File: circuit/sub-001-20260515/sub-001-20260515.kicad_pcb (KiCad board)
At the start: 2 copper layers, 114.3 x 107 mm, 148 parts, among them J1 Conn_NeoPixel, J2 Conn_SW_TGL, J3 Conn_Power, J4 Conn_Main, Q1 BSS138, Q2 BSS138, Q3 BSS138, Q4 BSS138, Q5 BSS138, Q6 BSS138, Q7 BSS138, Q8 BSS138, U11 LM1117GS-3.3, U12 NE555DR, U13 NE555DR, U14 LM1117GS-3.3, U15 LM1117GS-3.3, U18 NE555DR, U19 NE555DR, U2 LM1117GS-3.3, U20 TSSP58038, U21 TSSP58038, U22 NE555DR, U23 NE555DR, U24 TSSP58038, U25 TSSP58038, U26 HC-SR04, U27 HC-SR04, U28 HC-SR04, U29 HC-SR04, U4 NE555DR, U5 NE555DR, U7 LM1117GS-3.3, U9 LM1117MP-3.3

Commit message: Update サブ基板のPCBを進めた
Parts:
- moved U14 96.0 mm to (48.0, 0.00), turned to -90 degrees
- moved U7 96.0 mm to (-48.0, 0.00)
- moved U27 74.3 mm to (-37.0, 3.81), turned to 180 degrees
- moved U29 74.3 mm to (36.9, -3.81), turned to 0 degrees
- moved U3 64.4 mm to (-32.2, -1.17), turned to 180 degrees
- moved U8 64.4 mm to (32.2, -2.83), turned to 0 degrees

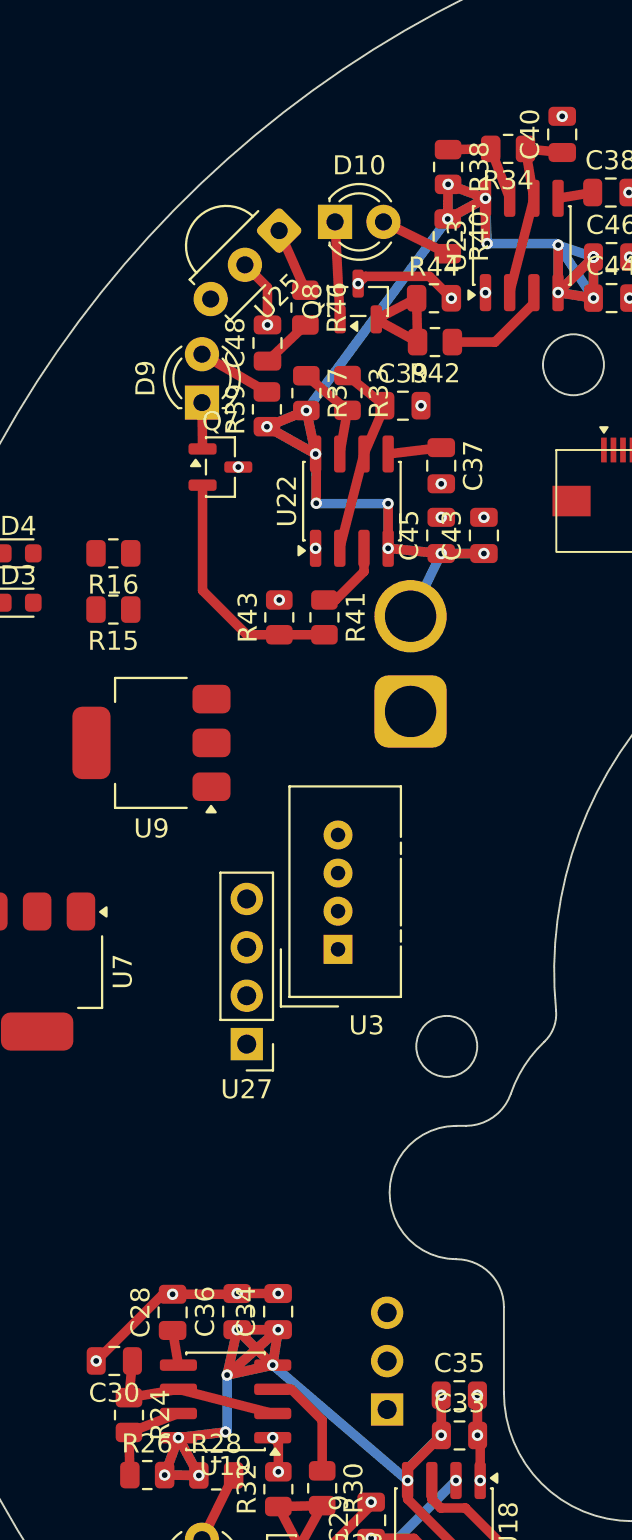
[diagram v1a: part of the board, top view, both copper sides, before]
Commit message: Update サブ基板のPCBを進めた
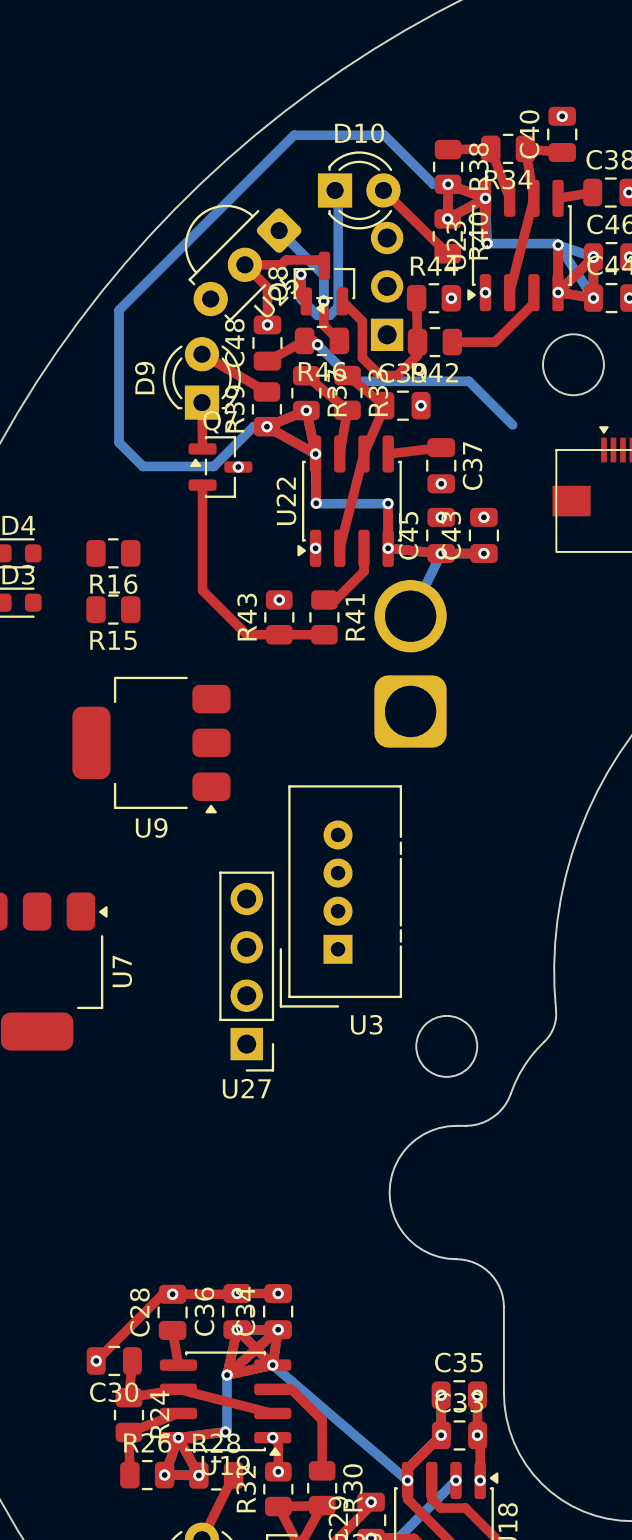
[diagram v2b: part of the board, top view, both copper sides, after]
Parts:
- moved J2 56.4 mm to (-29.6, -33.4)
- moved Q8 2.00 mm to (-32.9, -36.1)
- moved R46 1.95 mm to (-33.0, -33.1), turned to 180 degrees
- moved D10 1.65 mm to (-32.4, -41.0)
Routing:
- net +5V: track 370.8 -> 396.5 mm
- net IR_sig4: track 2.75 -> 15.0 mm, vias 0 -> 1
- net Net-(D10-K): track 5.12 -> 11.5 mm, vias 0 -> 1
- net Net-(U25-OUT): track 3.42 -> 7.10 mm, vias 0 -> 1
- net Net-(Q8-G): track 7.16 -> 10.1 mm
- net GND: track 79.1 -> 77.9 mm, vias 59 -> 58
- net Net-(D10-A): track 3.76 -> 4.73 mm

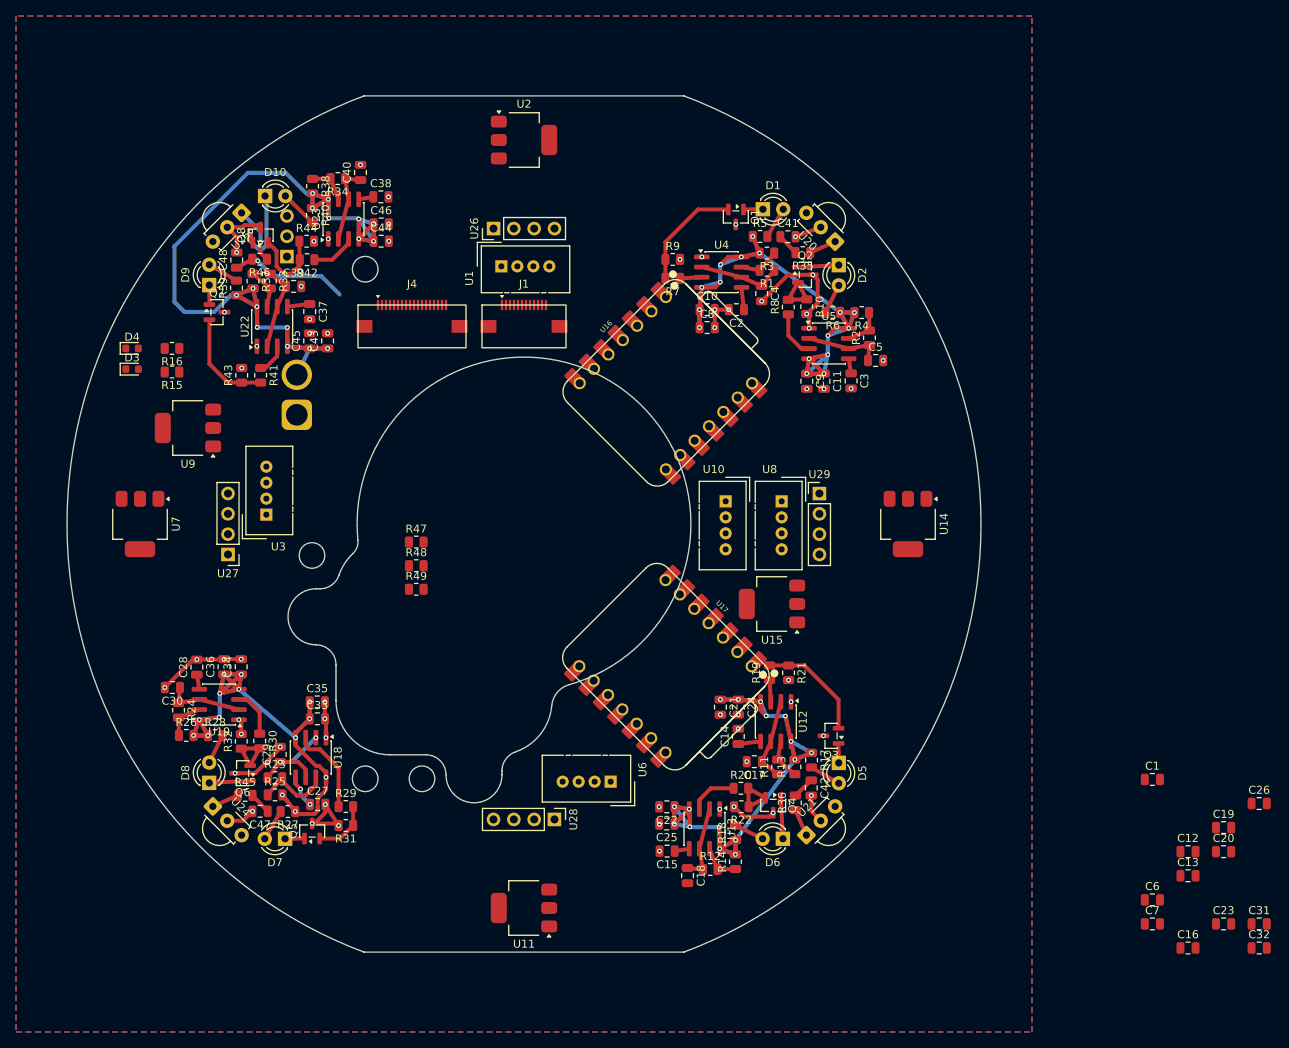
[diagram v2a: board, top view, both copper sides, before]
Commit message: Update サブ基板のFPCコネクタ周りを更新
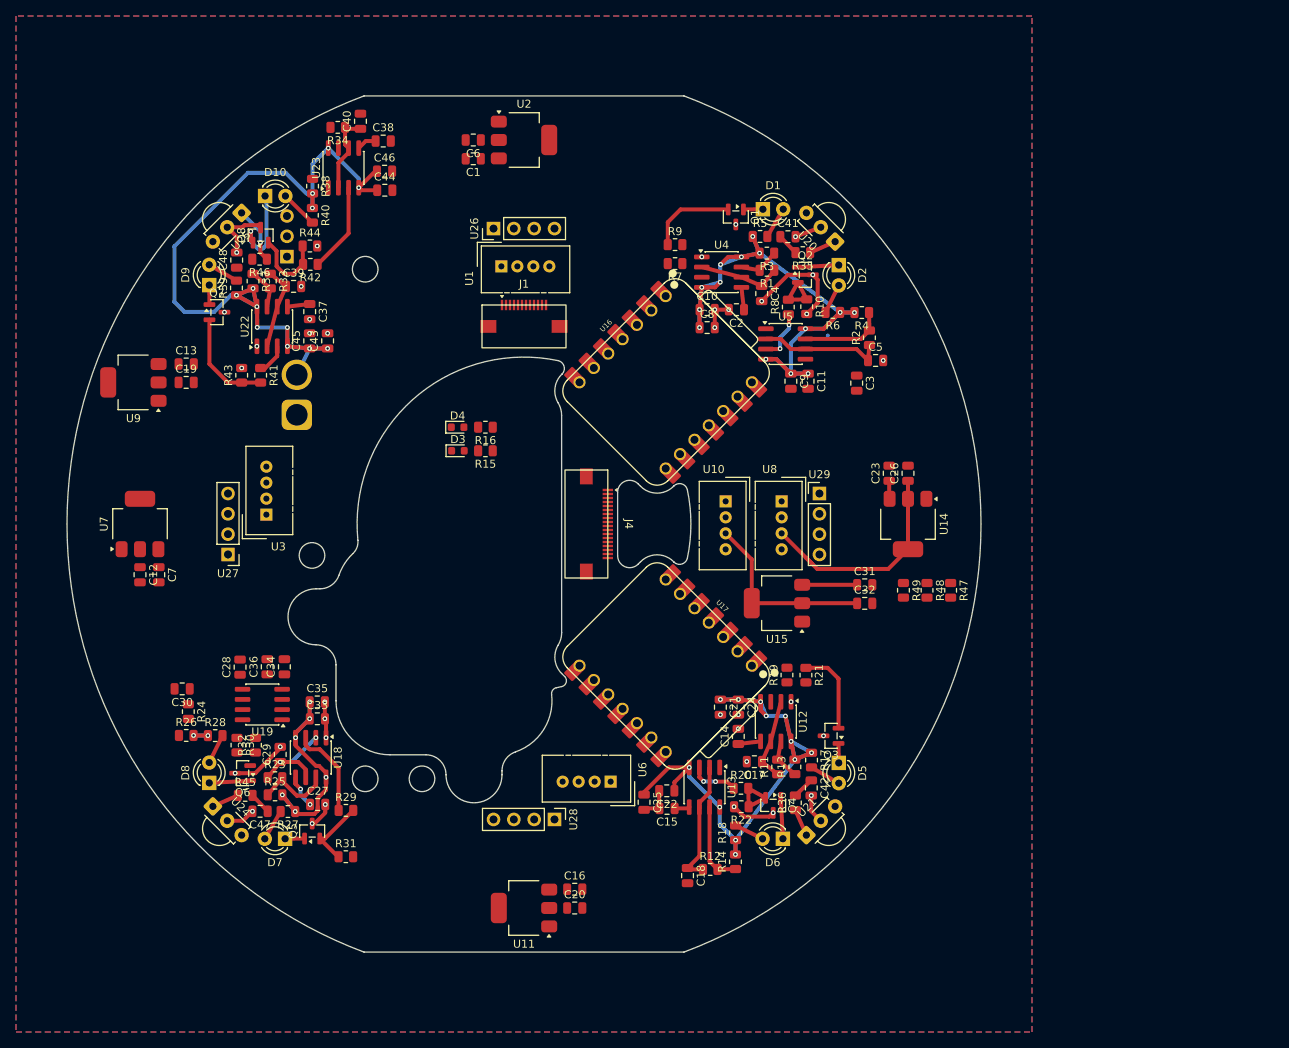
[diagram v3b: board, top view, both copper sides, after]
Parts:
- moved C19 141.1 mm to (-42.2, -17.7)
- moved C13 140.6 mm to (-42.2, -20.0)
- moved C12 135.5 mm to (-48.0, 6.34), turned to -90 degrees
- moved C7 131.6 mm to (-45.6, 6.34), turned to -90 degrees
- moved C6 127.4 mm to (-6.34, -48.0), turned to 180 degrees
- moved C1 115.0 mm to (-6.34, -45.6), turned to 180 degrees
- moved C20 81.4 mm to (6.34, 48.0)
- moved C16 77.0 mm to (6.34, 45.6)
- moved C23 70.1 mm to (45.6, -6.34), turned to 90 degrees
- moved R47 67.1 mm to (53.3, 8.29), turned to -90 degrees
- moved C32 65.5 mm to (42.6, 9.92)
- moved C31 65.0 mm to (42.6, 7.60)
- moved R48 63.9 mm to (50.4, 8.29), turned to -90 degrees
- moved R49 60.9 mm to (47.4, 8.29), turned to -90 degrees
- moved C26 60.3 mm to (48.0, -6.34), turned to 90 degrees
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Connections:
- C13 pad 2: Net-(C13-Pad2) -> GND
- C19 pad 2: Net-(C13-Pad2) -> GND
- J1 pad 1: +5V -> SIG_{NeoPixel}
- J1 pad 10: SW_{TCT3} -> +3.3V
- J1 pad 11: SW_{START} -> +5V
- J1 pad 12: SIG_{NeoPixel} -> +5V
- J1 pad 2: +5V -> SW_{START}
- J1 pad 3: +3.3V -> SW_{TCT3}
- J1 pad 4: GND -> SW_{TCT2}
- J1 pad 5: GND -> SW_{TCT1}
- J1 pad 6: SDA -> SCL
- J1 pad 7: SCL -> SDA
- J1 pad 8: SW_{TCT1} -> GND
- J1 pad 9: SW_{TCT2} -> GND
- J4 pad 1: TX_{teensy}-RX_{unitV2} -> RX_{teensy}-TX_{unitV4}
- J4 pad 10: GND -> RX_{teensy}-TX_{unitV5}
- J4 pad 11: GND -> SW_{START}
- J4 pad 12: GND -> TX_{teensy}-RX_{unitV5}
- J4 pad 13: RX_{teensy}-TX_{ESP32C301} -> TX_{teensy}-RX_{ESP32C302}
- J4 pad 14: TX_{teensy}-RX_{ESP32C301} -> RX_{teensy}-TX_{ESP32C302}
- J4 pad 15: RX_{teensy}-TX_{unitV3} -> RX_{teensy}-TX_{unitV1}
- J4 pad 16: TX_{teensy}-RX_{unitV3} -> TX_{teensy}-RX_{unitV1}
- J4 pad 17: TX_{teensy}-RX_{unitV4} -> RX_{teensy}-TX_{unitV2}
- J4 pad 18: RX_{teensy}-TX_{unitV4} -> TX_{teensy}-RX_{unitV2}
- J4 pad 2: RX_{teensy}-TX_{unitV2} -> TX_{teensy}-RX_{unitV4}
- J4 pad 3: TX_{teensy}-RX_{unitV1} -> TX_{teensy}-RX_{unitV3}
- J4 pad 4: RX_{teensy}-TX_{unitV1} -> RX_{teensy}-TX_{unitV3}
- J4 pad 5: RX_{teensy}-TX_{ESP32C302} -> TX_{teensy}-RX_{ESP32C301}
- J4 pad 6: TX_{teensy}-RX_{ESP32C302} -> RX_{teensy}-TX_{ESP32C301}
- J4 pad 7: TX_{teensy}-RX_{unitV5} -> GND
- J4 pad 8: SW_{START} -> GND
- J4 pad 9: RX_{teensy}-TX_{unitV5} -> GND
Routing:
- net +5V: track 396.5 -> 297.1 mm, vias 63 -> 46
- net 3.3V-unitV4: track 0.00 -> 28.3 mm
- net 3.3V-unitV5: track 0.00 -> 23.3 mm
- net GND: track 77.9 -> 61.2 mm, vias 58 -> 36
- net IR_sig4: track 15.0 -> 0.00 mm, vias 1 -> 0
- net Net-(U19-THRES): track 9.68 -> 0.00 mm
- net Net-(Q6-G): track 7.16 -> 0.00 mm
- net Net-(U5-THRES): track 9.68 -> 16.8 mm
- net Net-(U13-THRES): track 9.68 -> 16.3 mm
- net Net-(U19-OUT): track 5.93 -> 0.00 mm
- net Net-(U5-DISCH): track 5.02 -> 10.7 mm
- net Net-(U23-OUT): track 5.68 -> 11.2 mm
- net Net-(U13-DISCH): track 5.02 -> 10.4 mm
- net Net-(U19-DISCH): track 5.02 -> 0.00 mm
- net Net-(U23-DISCH): track 5.02 -> 0.00 mm
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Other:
- outline, holes or cut-outs redrawn

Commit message: Update サブ基板のコンポーネント仮配置
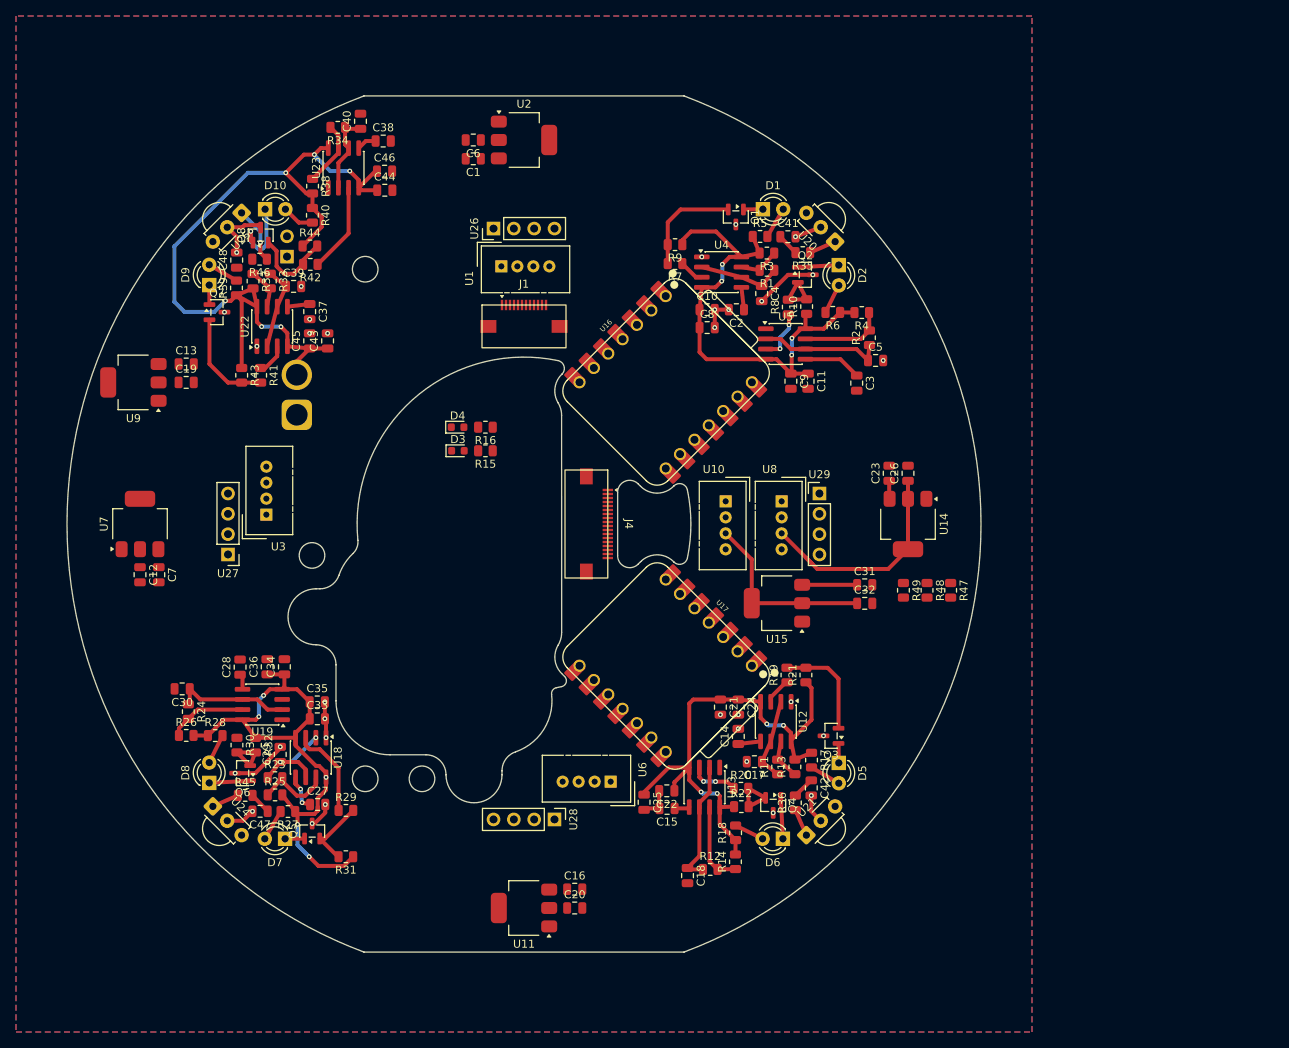
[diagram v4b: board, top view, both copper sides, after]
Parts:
- C21, C22, C33, C34, C43, C44, C8, C9: value 100n -> 10n
- C41, C42, C47, C48: value 10μ -> 0.33μ
- J2: value Conn_SW_TGL -> Conn_01x02_Socket; footprint Connector_PinSocket_2.54mm:PinSocket_1x03_P2.54mm_Vertical -> Connector_PinSocket_2.54mm:PinSocket_1x02_P2.54mm_Vertical
- R10, R21, R22, R31, R32, R43, R44, R9: value 100k -> 1k
- R13, R14, R25, R26, R3, R37, R38, R4: value 1k -> 1.5k
- moved D10 1.65 mm to (-32.4, -39.3)
- turned R10 to 90 degrees
- turned R22 to 0 degrees
- turned R21 to 90 degrees
- turned R31 to 180 degrees
- turned R32 to -90 degrees
- turned R43 to -90 degrees
- turned R9 to 180 degrees
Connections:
- J1 pad 10: +3.3V -> +5V
- J1 pad 3: SW_{TCT3} -> SW_{TCT2}
- J1 pad 4: SW_{TCT2} -> SW_{TCT1}
- J1 pad 5: SW_{TCT1} -> SCL
- J1 pad 6: SCL -> SDA
- J1 pad 7: SDA -> GND
- J1 pad 9: GND -> +3.3V
- R10 pad 1: Net-(Q2-G) -> +5V
- R10 pad 2: GND -> Net-(Q2-G)
- R21 pad 1: Net-(Q3-G) -> +5V
- R21 pad 2: GND -> Net-(Q3-G)
- R22 pad 1: Net-(Q4-G) -> +5V
- R22 pad 2: GND -> Net-(Q4-G)
- R31 pad 1: Net-(Q5-G) -> +5V
- R31 pad 2: GND -> Net-(Q5-G)
- R32 pad 1: Net-(Q6-G) -> +5V
- R32 pad 2: GND -> Net-(Q6-G)
- R43 pad 1: Net-(Q7-G) -> +5V
- R43 pad 2: GND -> Net-(Q7-G)
- R44 pad 1: Net-(Q8-G) -> +5V
- R44 pad 2: GND -> Net-(Q8-G)
- R9 pad 1: Net-(Q1-G) -> +5V
- R9 pad 2: GND -> Net-(Q1-G)
- U16 pad 10: SW_{TCT2} -> unconnected-(U16-MISO_D9-Pad10)_1
- U16 pad 11: SW_{TCT3} -> SW_{TCT2}
- U17 pad 10: SW_{TGL3} -> unconnected-(U17-MISO_D9-Pad10)
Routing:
- net Net-(U19-THRES): track 0.00 -> 14.6 mm
- net GND: track 61.2 -> 49.5 mm, vias 36 -> 32
- net Net-(U19-DISCH): track 0.00 -> 9.81 mm
- net Net-(U23-DISCH): track 0.00 -> 8.19 mm
- net Net-(U5-CONT): track 0.00 -> 7.25 mm
- net Net-(Q6-G): track 0.00 -> 6.41 mm
- net +5V: track 297.1 -> 302.2 mm, vias 46 -> 19
- net Net-(U12-OUT): track 0.00 -> 3.36 mm
- net Net-(U4-OUT): track 0.00 -> 3.14 mm
- net Net-(Q3-G): track 10.8 -> 13.2 mm
- net Net-(Q1-G): track 11.0 -> 13.4 mm
- net Net-(U19-CONT): track 0.00 -> 1.94 mm
- net Net-(D10-K): track 11.5 -> 9.85 mm
- net Net-(Q8-G): track 9.87 -> 10.6 mm
- net Net-(D10-A): track 4.73 -> 4.06 mm

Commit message: Update サブ基板PCB完成。DRおなしゃあす
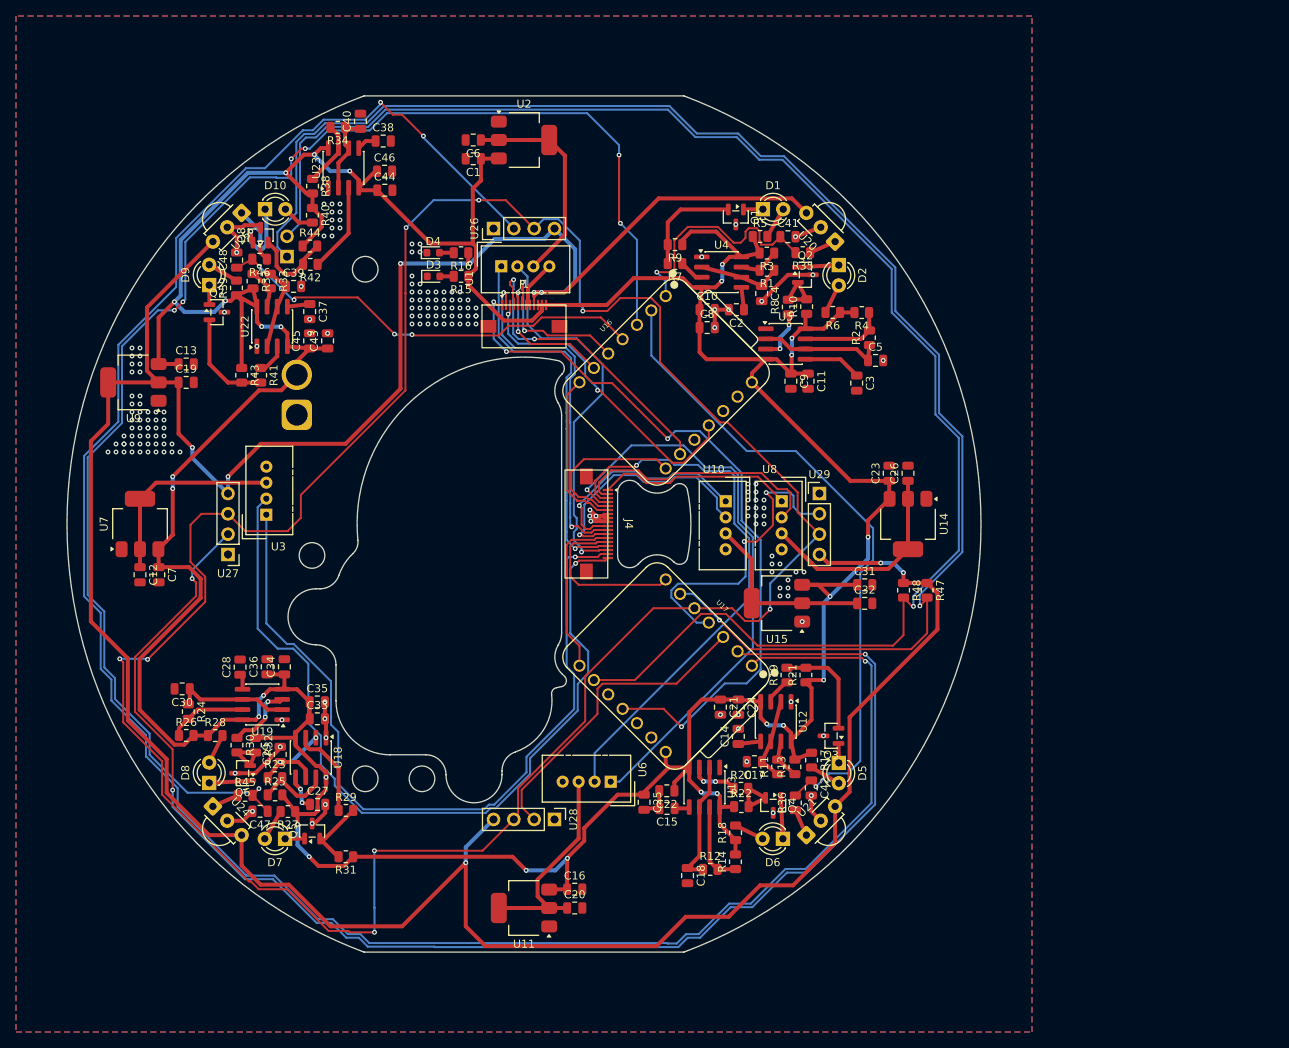
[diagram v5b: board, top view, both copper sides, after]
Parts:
- removed R49: 10k, Resistor_SMD:R_0805_2012Metric
- moved D3 22.0 mm to (-11.3, -31.0)
- moved R15 22.0 mm to (-7.87, -31.0)
- moved D4 22.0 mm to (-11.3, -33.9)
- moved R16 22.0 mm to (-7.87, -33.9)
- moved R48 2.94 mm to (47.4, 8.29)
- moved R47 2.94 mm to (50.4, 8.29)
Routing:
- net +3.3V: track 0.00 -> 397.5 mm, vias 0 -> 9
- net USS_{EN}: track 0.00 -> 308.5 mm, vias 0 -> 8
- net USS1: track 0.00 -> 270.8 mm, vias 0 -> 3
- net +5V: track 302.2 -> 553.9 mm, vias 19 -> 27
- net SW_{TGL2}: track 0.00 -> 194.9 mm, vias 0 -> 1
- net SW_{TGL1}: track 0.00 -> 189.3 mm, vias 0 -> 2
- net USS2: track 0.00 -> 179.1 mm, vias 0 -> 3
- net IR_sig3: track 2.75 -> 180.5 mm, vias 0 -> 7
- net TX_{teensy}-RX_{unitV2}: track 0.00 -> 104.1 mm, vias 0 -> 1
- net RX_{teensy}-TX_{unitV2}: track 0.00 -> 99.6 mm, vias 0 -> 1
- net SIG_{NeoPixel}: track 0.00 -> 91.2 mm, vias 0 -> 4
- net IR_sig2: track 2.75 -> 82.7 mm, vias 0 -> 1
- net RX_{teensy}-TX_{unitV3}: track 0.00 -> 73.4 mm, vias 0 -> 1
- net TX_{teensy}-RX_{unitV3}: track 0.00 -> 69.7 mm, vias 0 -> 1
- net IR_sig4: track 0.00 -> 54.9 mm, vias 0 -> 4
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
